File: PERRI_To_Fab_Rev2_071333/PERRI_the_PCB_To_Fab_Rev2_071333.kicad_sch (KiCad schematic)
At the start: 40 parts, among them J1 SS5-80-3.00-X-D-K-XX, J2 Conn_01x02, J3 Conn_02x50_Counter_Clockwise, J4 Conn_02x05_Counter_Clockwise, J5 SS5-80-3.00-X-D-K-XX, J6 Conn_01x03, J7 Conn_01x03, J8 Conn_01x03, SW2 SW_DIP_x08, U1 TMP441AIDCNR, U2 TPS2595, U3 PCA9554ADB, U4 NCV8508

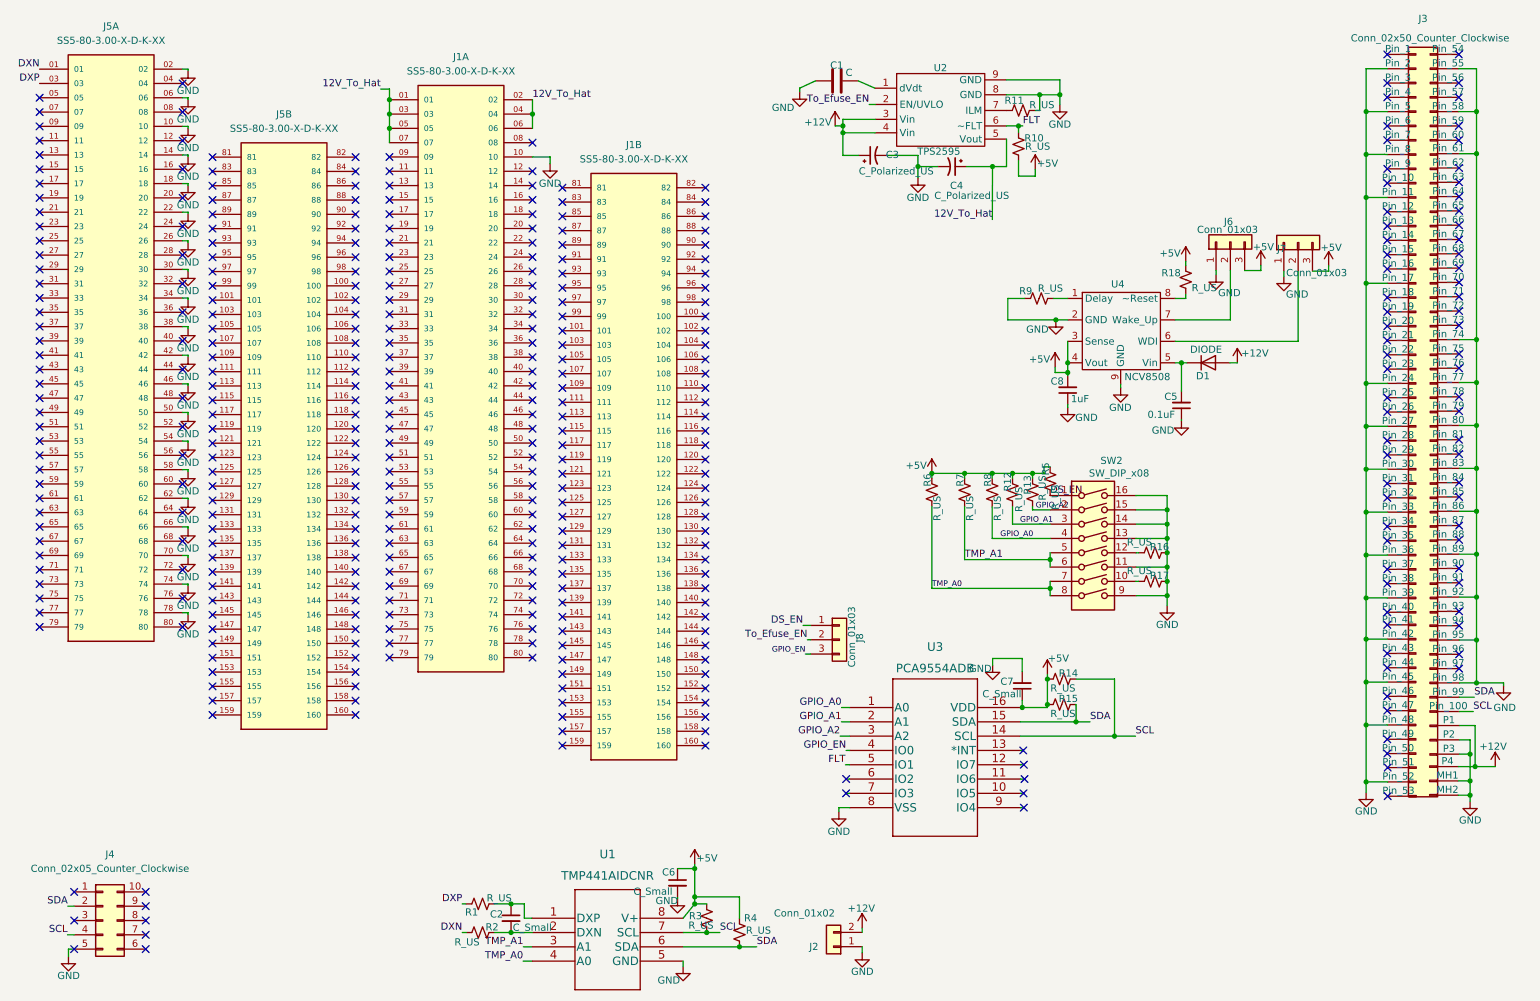
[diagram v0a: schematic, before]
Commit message: Changed the two 160 pin conn to one 20 pin conn
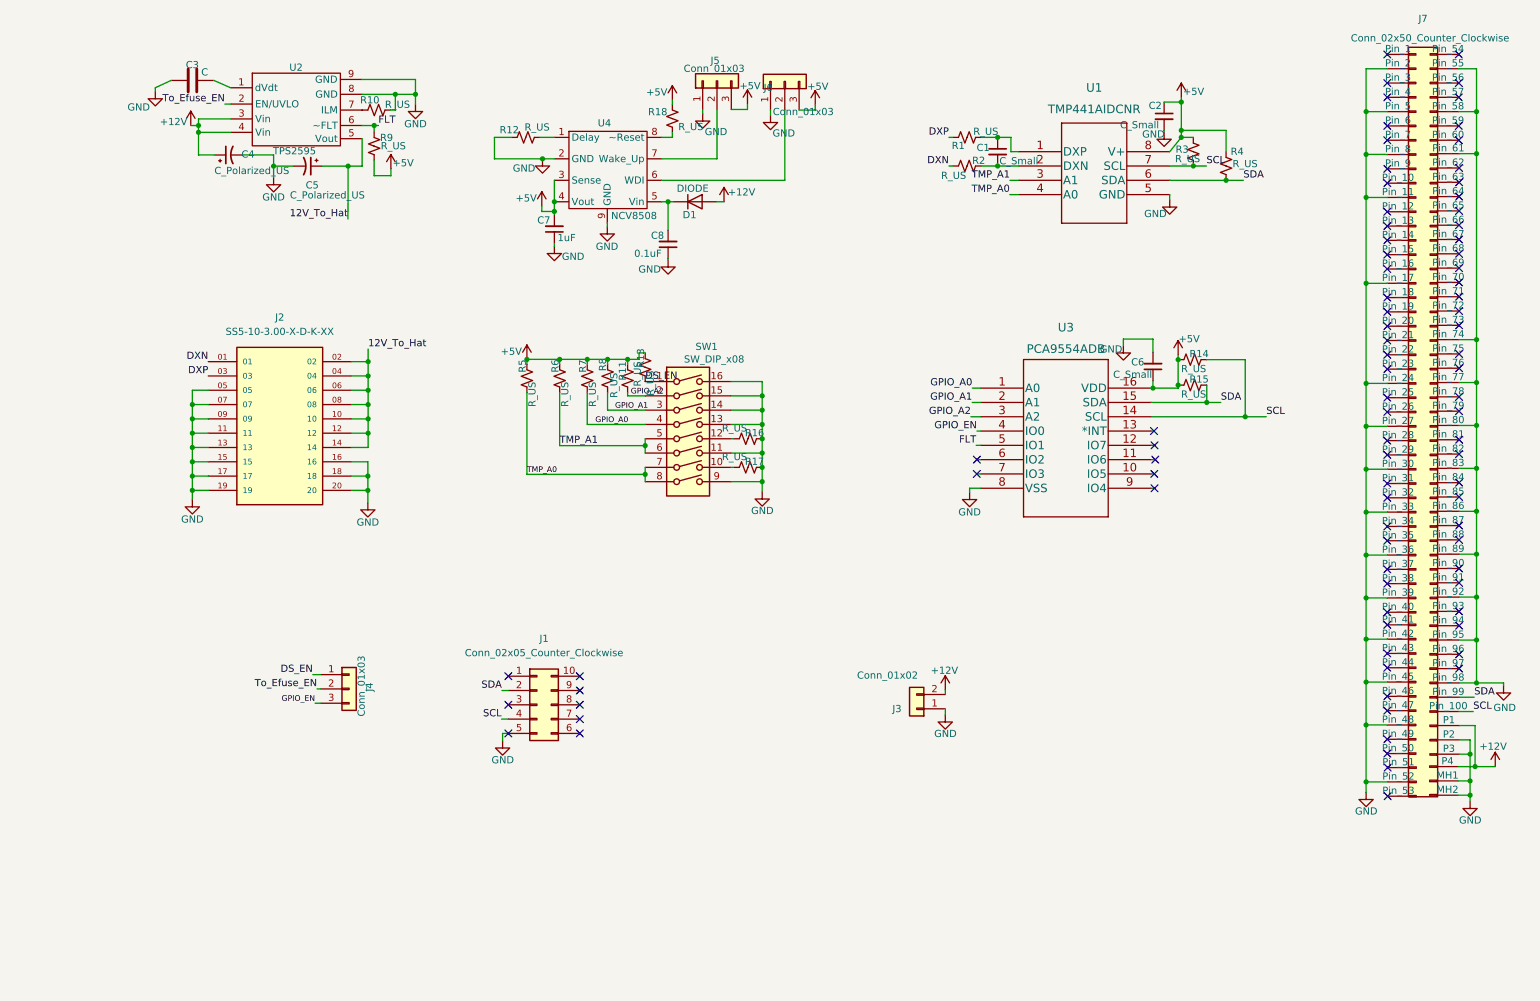
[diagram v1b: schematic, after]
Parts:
- removed J1, J5: SS5-80-3.00-X-D-K-XX, footprints:SAMTEC_SS5-80-3.00-X-D-K-XX, symbol SS5-80-3.00-X-D-K-XX:SS5-80-3.00-X-D-K-XX
- added J2: SS5-10-3.00-X-D-K-XX, footprints:SAMTEC_SS5-10-3.00-X-D-K-XX, symbol SS5-10-3.00-X-D-K-XX:SS5-10-3.00-X-D-K-XX
- renumbered C2 to C1, C6 to C2, C1 to C3, C3 to C4, C4 to C5, C7 to C6, C8 to C7, C5 to C8, J4 to J1, J2 to J3, J8 to J4, J6 to J5, J7 to J6, J3 to J7, R11 to R10, R13 to R11, R9 to R12, R5 to R13, R6 to R5, R7 to R6, R8 to R7, R12 to R8, R10 to R9, SW2 to SW1
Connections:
- net 12V_To_Hat: now also J2.02, J2.04, J2.06, J2.08, J2.10, J2.12, J2.14
- net DXN: now also J2.01
- net DXP: now also J2.03
- net GND: now also J2.05, J2.07, J2.09, J2.11, J2.13, J2.15, J2.16, J2.17, J2.18, J2.19, J2.20
- no-connect marks 376 -> 86
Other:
- moved on the sheet: C1, C2, C3, C4, C5, C6, C7, C8, D1, J1, J3, J4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
